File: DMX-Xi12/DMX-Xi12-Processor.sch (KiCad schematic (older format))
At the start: 27 parts, among them U1 LPC11U68JBD100E

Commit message: working on pcb
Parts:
- C10, C11, C12, C13, C14, C15, C16, C17, C3, C4, C5, C6, C7, C8, C9: renamed from C?; footprint (none) -> Capacitors_SMD:C_0603
- Con1: renamed from Con?; footprint (none) -> Components:Cortex-10-SWD
- P3: renamed from P?; footprint (none) -> Connect:USB_Mini-B
- R1, R2, R3, R4, R5: renamed from R?; footprint (none) -> Resistors_SMD:R_0603
- SW2: renamed from SW?; footprint (none) -> Buttons_Switches_ThroughHole:SW_DIP_x4_Slide
- SW3, SW4: renamed from SW?; footprint (none) -> Buttons_Switches_ThroughHole:SW_TH_Tactile_Omron_B3F-10xx
- U2: renamed from U1; footprint (none) -> Housings_QFP:LQFP-100_14x14mm_Pitch0.5mm
- Y1: renamed from Y?; footprint (none) -> Crystals:Crystal_HC49-SD_SMD

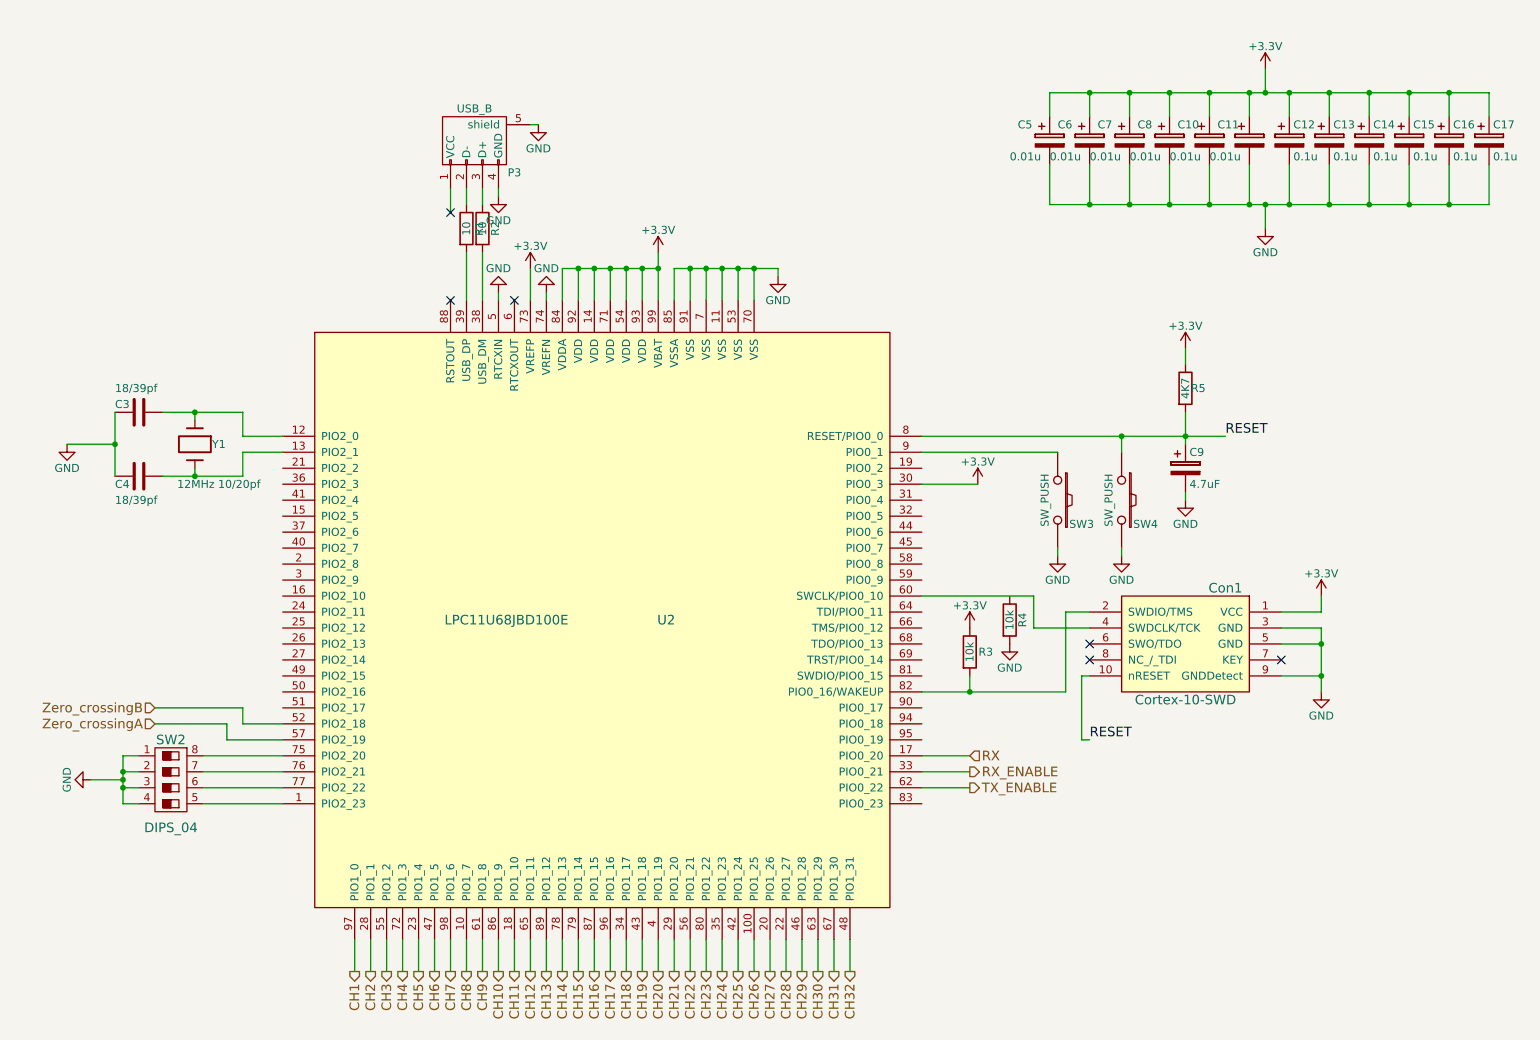
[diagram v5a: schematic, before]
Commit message: completed board. Schematic, is correct but some part values and numbers need updating! Do not trust the schematic yet
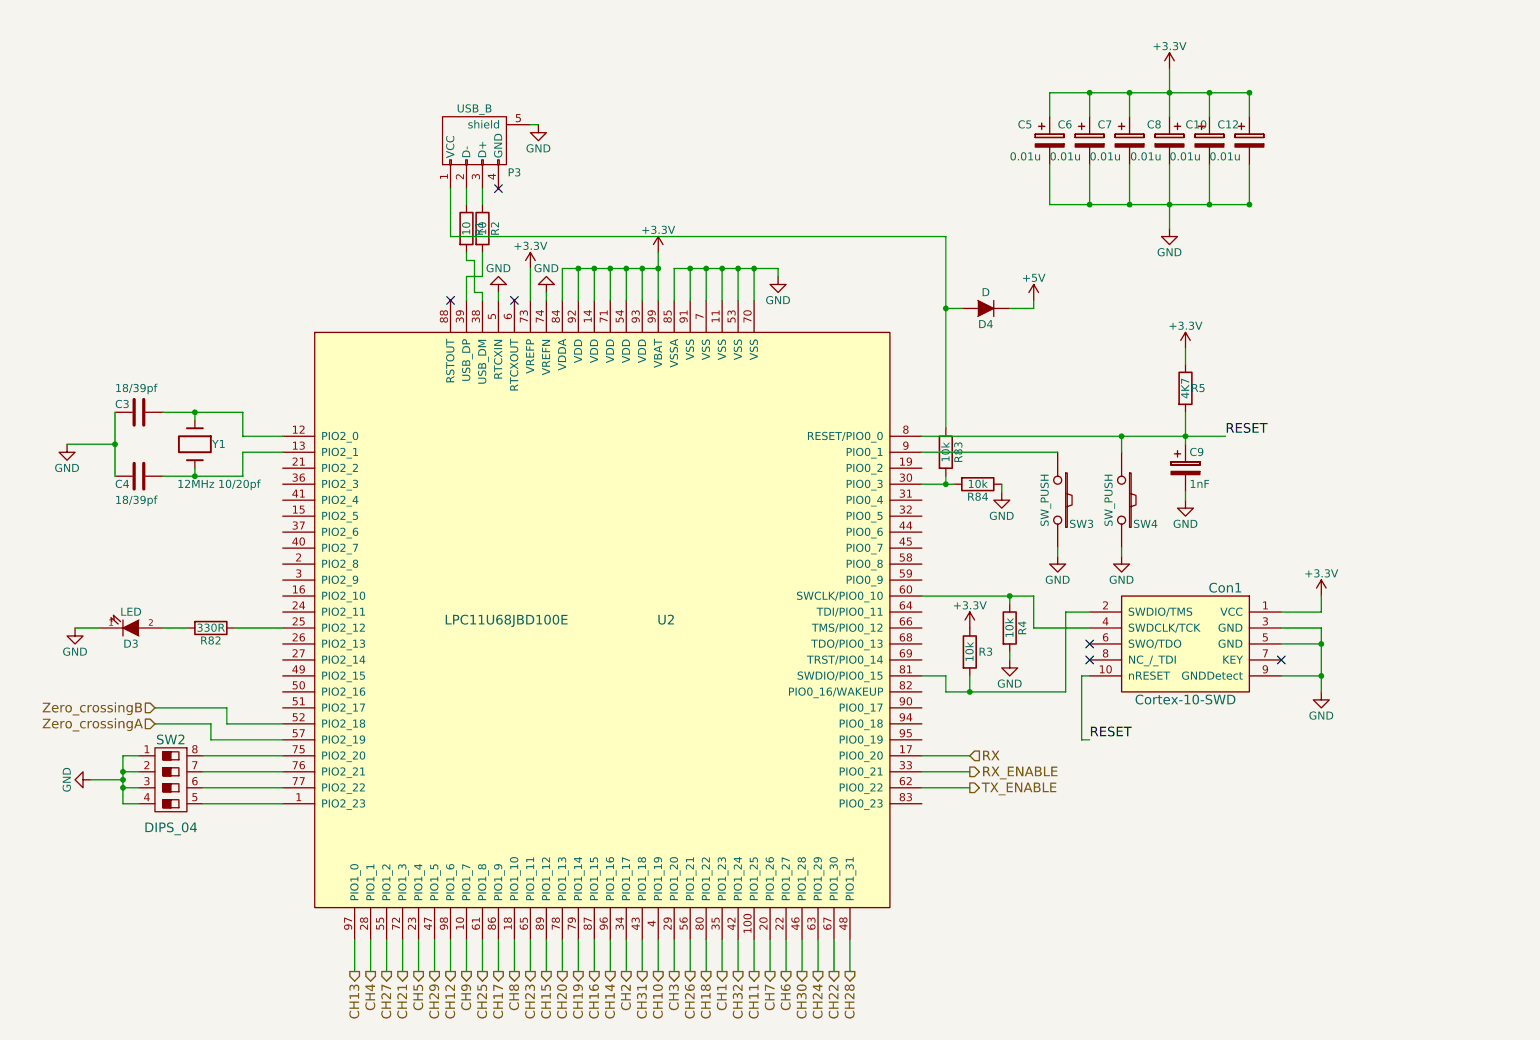
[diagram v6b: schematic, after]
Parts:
- removed C12, C13, C14, C15, C16, C17: 0.1u, Capacitors_SMD:C_0603, symbol CP
- added D3: LED, LEDs:LED_0603, symbol LED
- added D4: D, Diodes_ThroughHole:Diode_DO-41_SOD81_Horizontal_RM10, symbol D
- added R82: 330R, Resistors_SMD:R_0603, symbol R
- added R83, R84: 10k, Resistors_SMD:R_0603, symbol R
- C9: value 4.7uF -> 1nF
- renumbered C11 to C12
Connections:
- net +3V3: no longer U2.30 (PIO0_3)
- net CH1: now also U2.35 (PIO1_23); no longer U2.97 (PIO1_0)
- net CH10: now also U2.4 (PIO1_19); no longer U2.86 (PIO1_9)
- net CH11: now also U2.100 (PIO1_25); no longer U2.18 (PIO1_10)
- net CH12: now also U2.98 (PIO1_6); no longer U2.65 (PIO1_11)
- net CH13: now also U2.97 (PIO1_0); no longer U2.89 (PIO1_12)
- net CH14: now also U2.96 (PIO1_16); no longer U2.78 (PIO1_13)
- net CH15: now also U2.89 (PIO1_12); no longer U2.79 (PIO1_14)
- net CH17: now also U2.86 (PIO1_9); no longer U2.96 (PIO1_16)
- net CH18: now also U2.80 (PIO1_22); no longer U2.34 (PIO1_17)
- net CH19: now also U2.79 (PIO1_14); no longer U2.43 (PIO1_18)
- net CH2: now also U2.34 (PIO1_17); no longer U2.28 (PIO1_1)
- net CH20: now also U2.78 (PIO1_13); no longer U2.4 (PIO1_19)
- net CH21: now also U2.72 (PIO1_3); no longer U2.29 (PIO1_20)
- net CH22: now also U2.67 (PIO1_30); no longer U2.56 (PIO1_21)
- net CH23: now also U2.65 (PIO1_11); no longer U2.80 (PIO1_22)
- net CH24: now also U2.63 (PIO1_29); no longer U2.35 (PIO1_23)
- net CH25: now also U2.61 (PIO1_8); no longer U2.42 (PIO1_24)
- net CH26: now also U2.56 (PIO1_21); no longer U2.100 (PIO1_25)
- net CH27: now also U2.55 (PIO1_2); no longer U2.20 (PIO1_26)
- net CH28: now also U2.48 (PIO1_31); no longer U2.22 (PIO1_27)
- net CH29: now also U2.47 (PIO1_5); no longer U2.46 (PIO1_28)
- net CH3: now also U2.29 (PIO1_20); no longer U2.55 (PIO1_2)
- net CH30: now also U2.46 (PIO1_28); no longer U2.63 (PIO1_29)
- net CH31: now also U2.43 (PIO1_18); no longer U2.67 (PIO1_30)
- net CH32: now also U2.42 (PIO1_24); no longer U2.48 (PIO1_31)
- net CH4: now also U2.28 (PIO1_1); no longer U2.72 (PIO1_3)
- net CH6: now also U2.22 (PIO1_27); no longer U2.47 (PIO1_5)
- net CH7: now also U2.20 (PIO1_26); no longer U2.98 (PIO1_6)
- net CH8: now also U2.18 (PIO1_10); no longer U2.10 (PIO1_7)
- net CH9: now also U2.10 (PIO1_7); no longer U2.61 (PIO1_8)
- net GND: now also D3.1 (K), R84.1; no longer P3.4 (GND)
- net at U2.25 (PIO2_12): now also R82.1
- net at U2.38 (USB_DM): now also R1.2; no longer R2.2
- net at U2.39 (USB_DP): now also R2.2; no longer R1.2
- net at Con1.4 (SWDCLK/TCK), U2.60 (SWCLK/PIO0_10): now also R4.1
- net at U2.81 (SWDIO/PIO0_15): now also Con1.2 (SWDIO/TMS), R3.2
- net at P3.1 (VCC): now also D4.2 (A), R83.1
- new net: R83.2, R84.2, U2.30 (PIO0_3)
- new net: D3.2 (A), R82.2
- new net +5V: D4.1 (K)
- now unconnected: U2.82 (PIO0_16/WAKEUP)
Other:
- moved on the sheet: R4
